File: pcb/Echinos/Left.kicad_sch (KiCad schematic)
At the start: 30 parts, among them J1 USB_C_Receptacle_USB2.0, J2 FPC (PCB), J206 Conn_01x06_Pin, J4 FPC_VIK, J5 SATA-7p, U3 ESD7L5.0DT5G-N, U5 XC6210B332MR-G, U7 SRV05-4

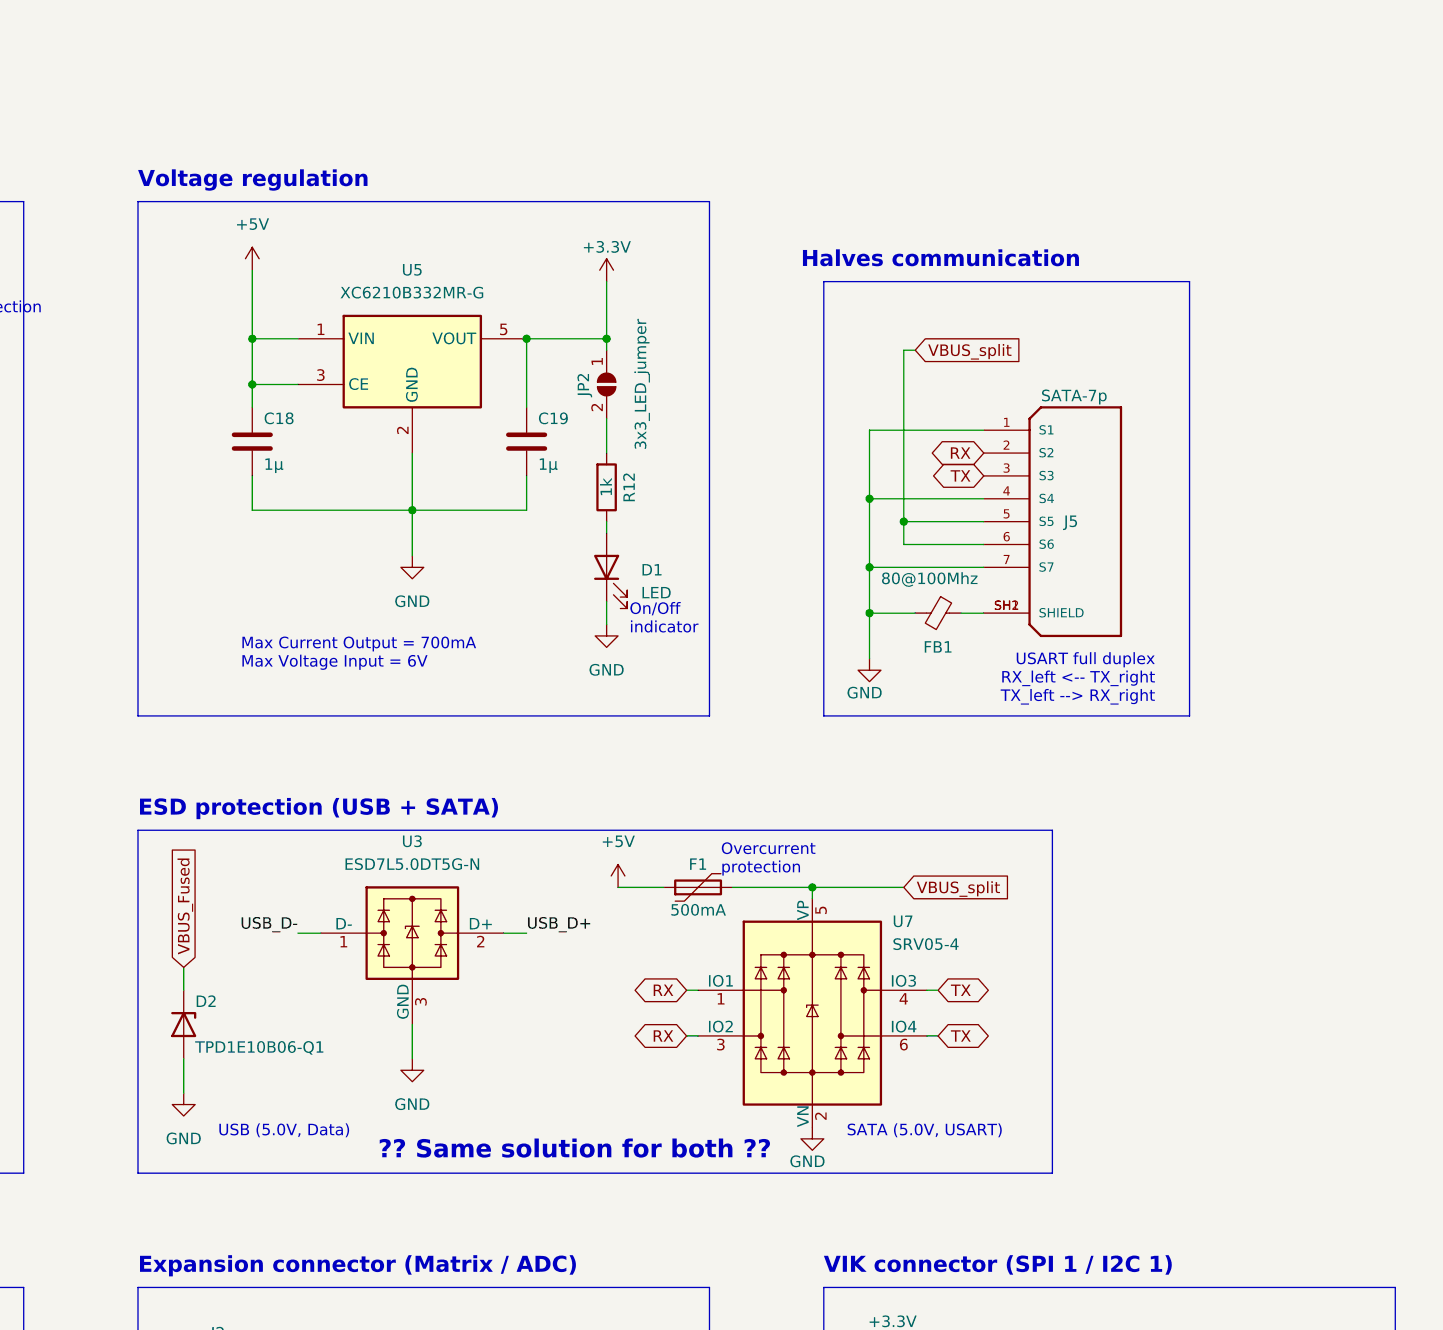
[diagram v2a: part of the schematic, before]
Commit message: ♻️ [PCB] - Now using the same ESD protection on both SATA and USB. Add ground fill and earth fill using ferrite bead as gate between both.
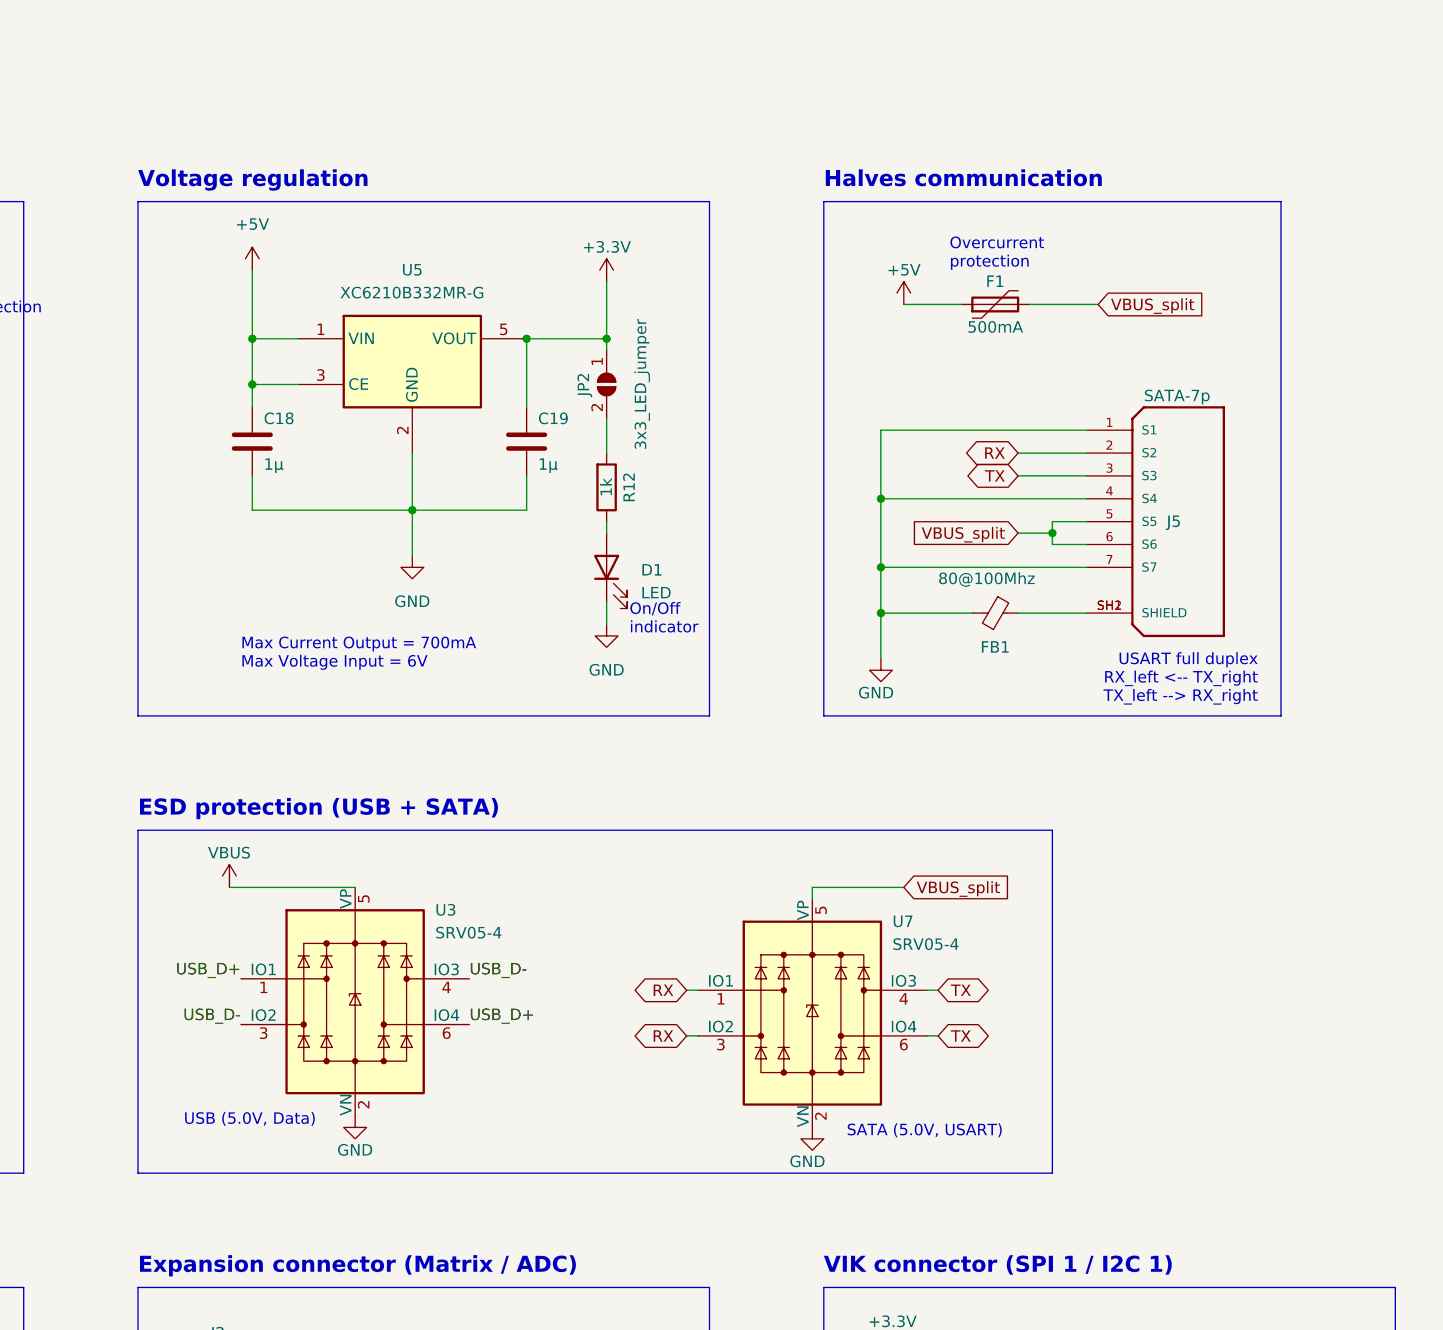
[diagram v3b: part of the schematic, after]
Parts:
- removed D2: TPD1E10B06-Q1, Diode_SMD:D_SOD-523, symbol Diode:BZT52Bxx
- removed U3: ESD7L5.0DT5G-N, Echinos:D_TVS_SOT-723, symbol Power_Protection:TPD2EUSB30
- added U3: SRV05-4, Package_TO_SOT_SMD:SOT-23-6, symbol Power_Protection:SRV05-4
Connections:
- net GND: now also U3.2 (VN)
- net USB_D+: now also U3.1 (IO1), U3.6 (IO4)
- net USB_D-: now also U3.3 (IO2), U3.4 (IO3)
- net VBUS: now also U3.5 (VP)
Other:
- note removed: "?? Same solution for both ??"
